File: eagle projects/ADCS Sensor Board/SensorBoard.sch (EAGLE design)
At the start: 128 parts, among them Q3 CSTCR4M00G15L99, Q5 32.768kHz, U10 LMV321, U2 ADS7841E_2K5, U3 LMV321, U5 ADS7841E_2K5, U6 REF194GSZ-REEL7, U7 TLV9054IDR, U8 LMV321

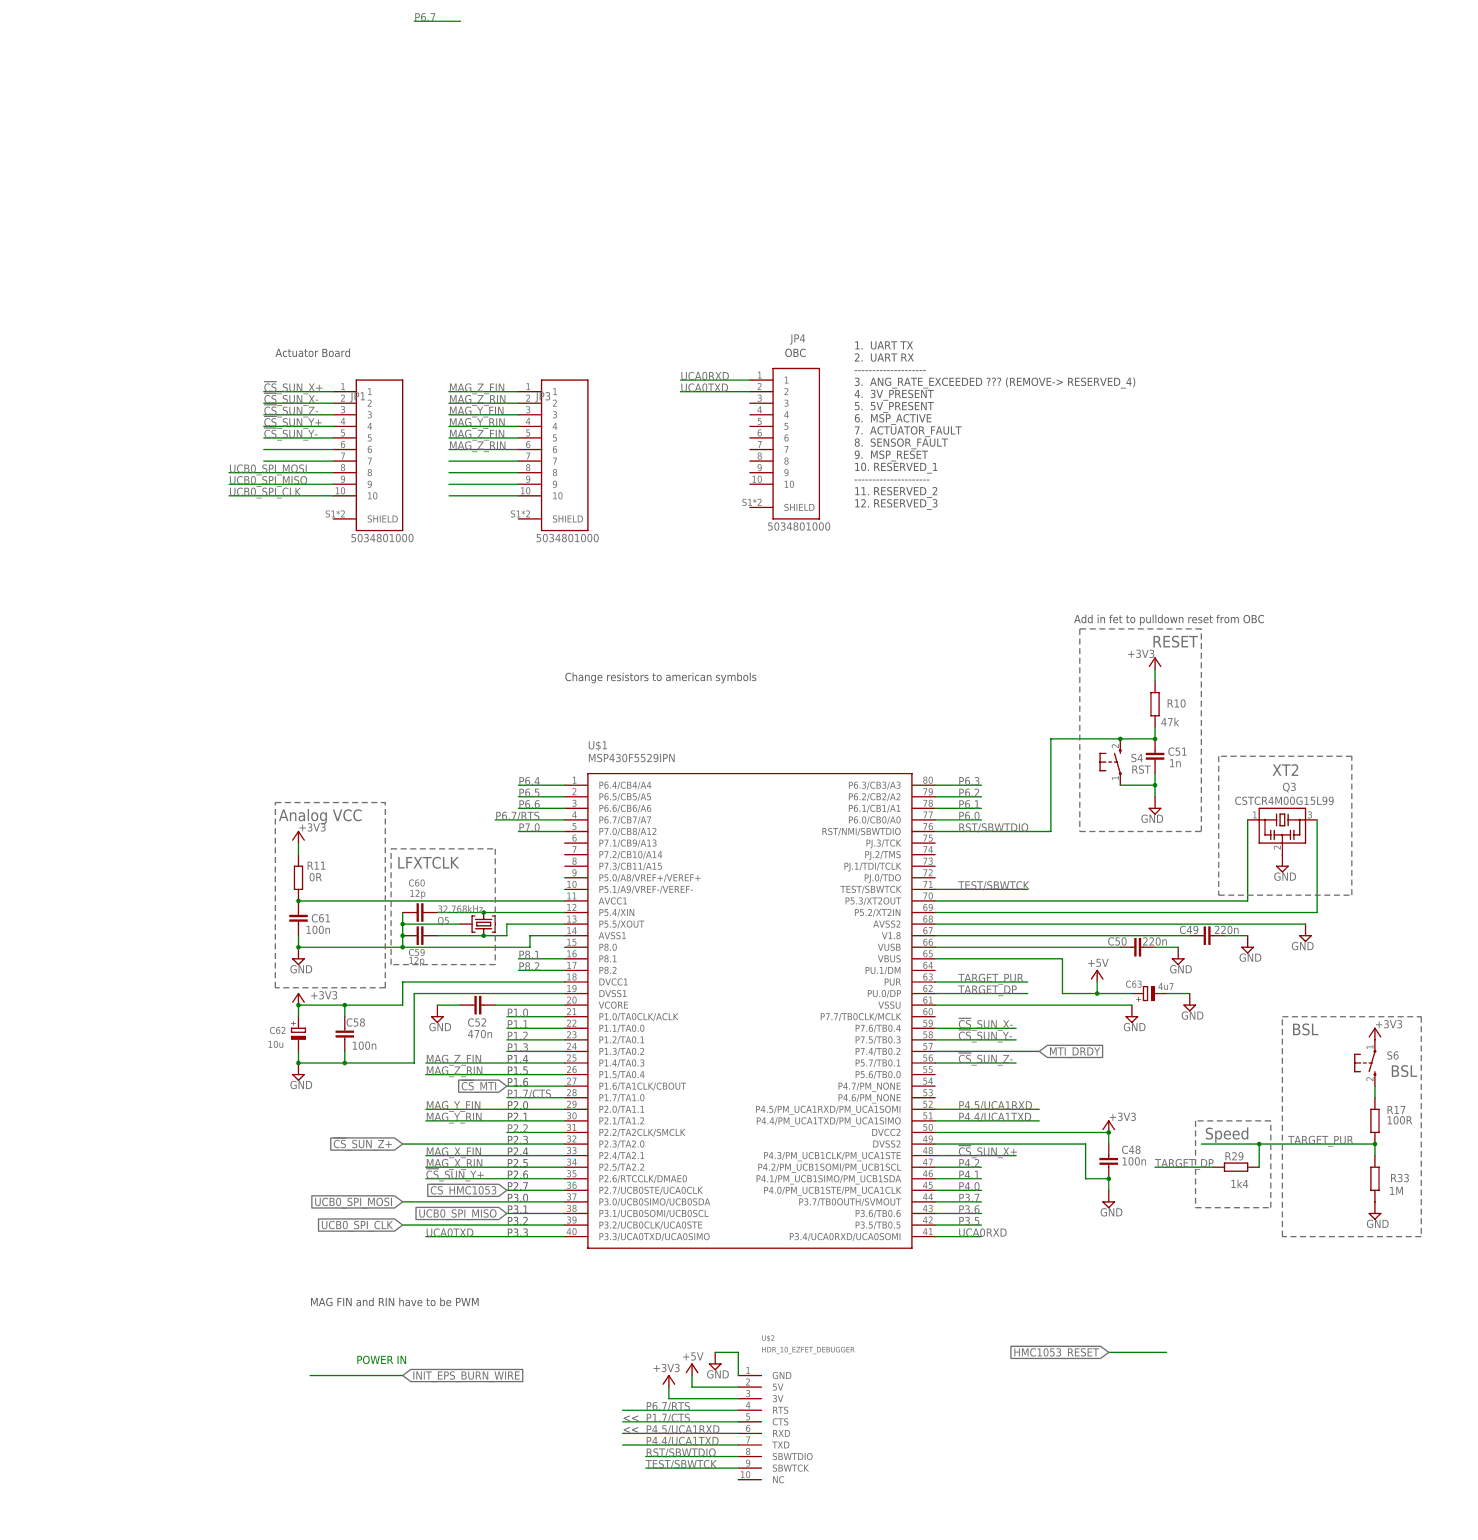
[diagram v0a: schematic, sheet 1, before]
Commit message: Renamed sensor board files. Added notes to schematic for remaining work
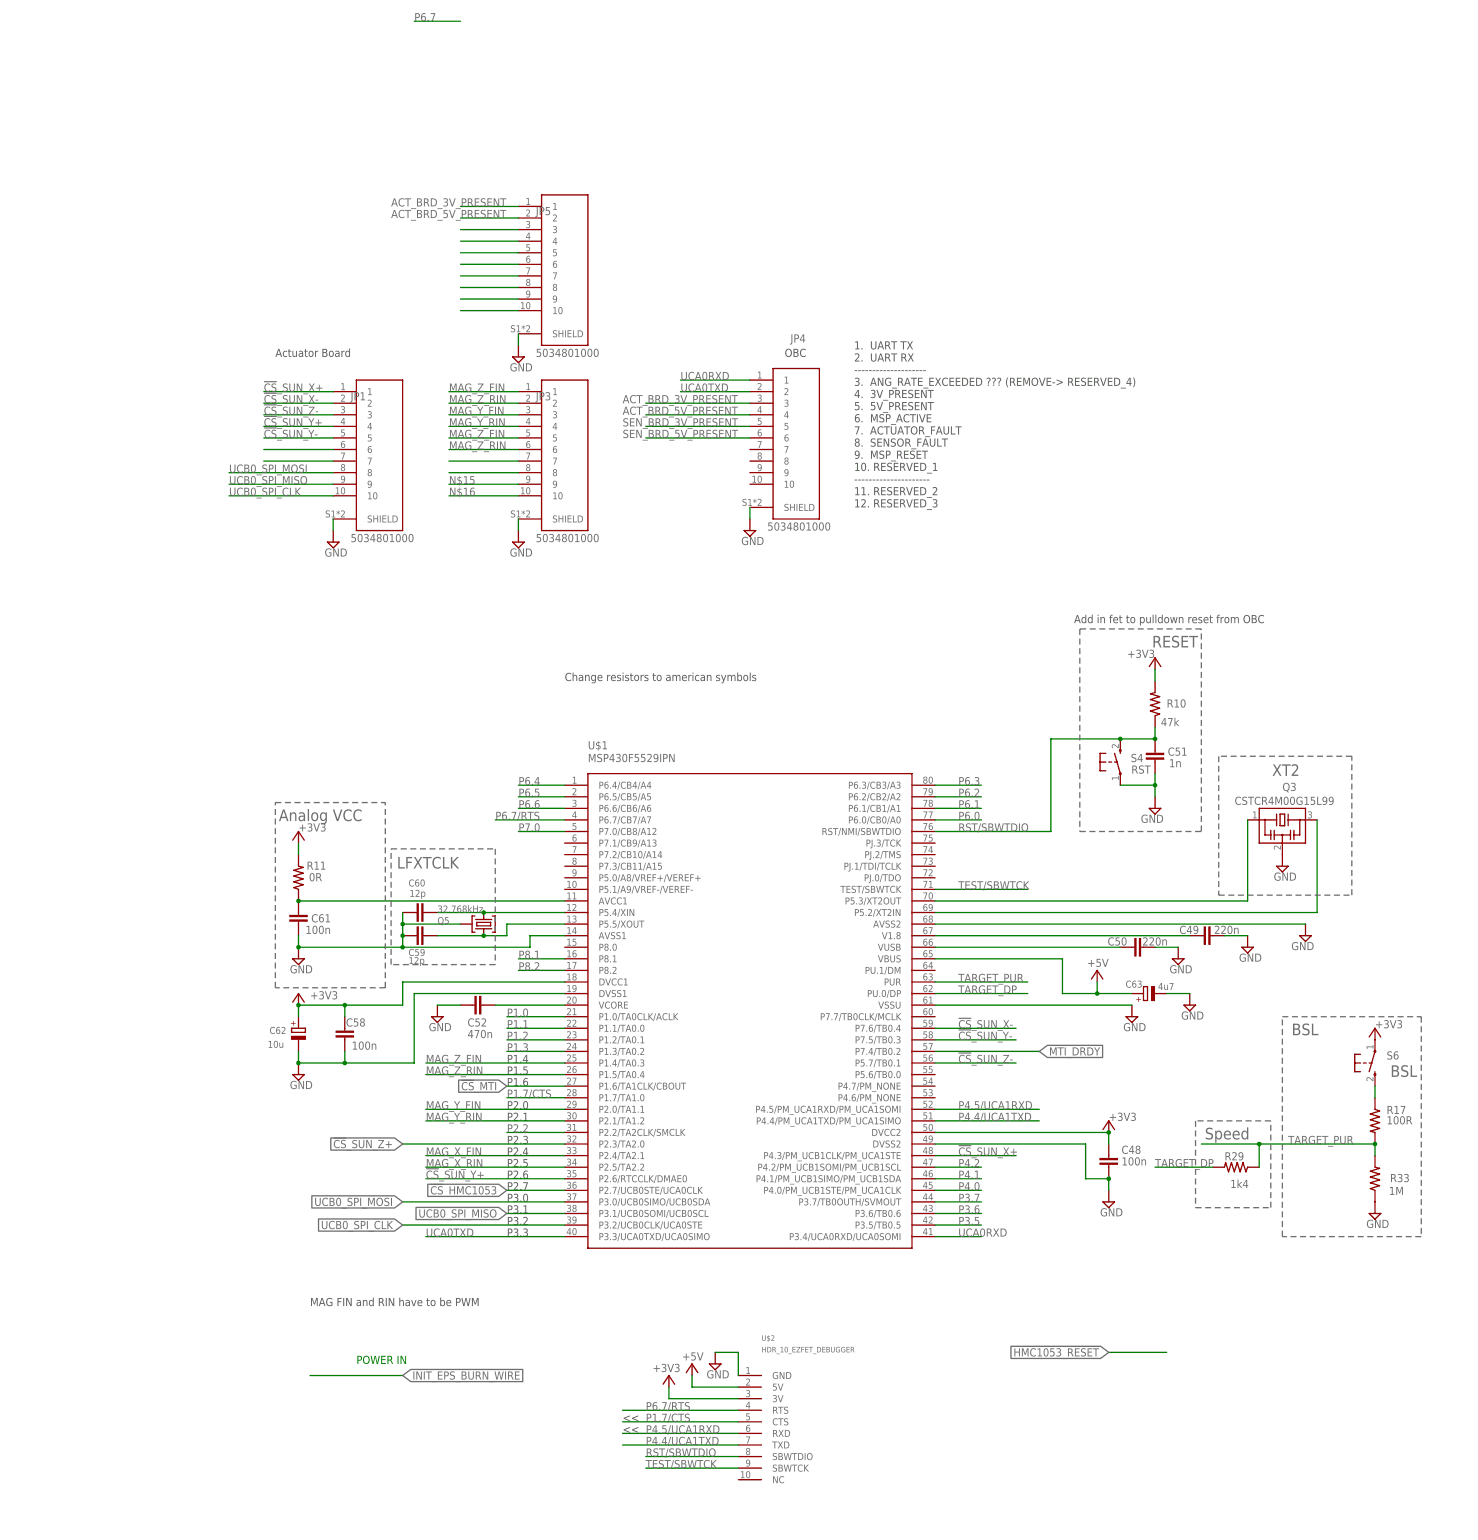
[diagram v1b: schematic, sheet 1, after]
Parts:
- added JP5: 5034801000, my_library:5034801000
- R10, R11, R17, R29, R33: device rcl:R-EU_RM0402 -> rcl:R-US_R0402
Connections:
- new net ACT_BRD_3V_PRESENT: JP4.3, JP5.1
- new net ACT_BRD_5V_PRESENT: JP4.4, JP5.2
- new net N$10: JP5.7
- new net N$17: JP5.8
- new net N$18: JP5.9
- new net N$19: JP5.10
- new net N$3: JP5.3
- new net N$4: JP5.4
- new net N$5: JP5.5
- new net N$9: JP5.6
- new net SEN_BRD_3V_PRESENT: JP4.5
- new net SEN_BRD_5V_PRESENT: JP4.6
- net GND: now also JP1.SHIELD, JP3.SHIELD, JP4.SHIELD, JP5.SHIELD
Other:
- note added: "Replace MTI-1 IMU with new 3-axis gyroscope"
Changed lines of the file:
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@@
 <part name="C49" library="rcl" deviceset="C-EU" device="CM0402" value="220n"/>
 <part name="C50" library="rcl" deviceset="C-EU" device="CM0402" value="220n"/>
-<part name="R10" library="rcl" deviceset="R-EU_" device="RM0402" value="47k"/>
+<part name="R10" library="rcl" library_urn="urn:adsk.eagle:library:334" deviceset="R-US_" device="R0402" package3d_urn="urn:adsk.eagle:package:23547/3" value="47k"/>
 <part name="C51" library="rcl" deviceset="C-EU" device="CM0402" value="1n"/>
 <part name="C52" library="rcl" deviceset="C-EU" device="CM0402" value="470n"/>
 <part name="C58" library="rcl" deviceset="C-EU" device="CM0402" value="100n"/>
-<part name="R11" library="rcl" deviceset="R-EU_" device="RM0402" value="0R"/>
+<part name="R11" library="rcl" library_urn="urn:adsk.eagle:library:334" deviceset="R-US_" device="R0402" package3d_urn="urn:adsk.eagle:package:23547/3" value="0R"/>
 <part name="C59" library="rcl" deviceset="C-EU" device="CM0402" value="12p"/>
 <part name="C60" library="rcl" deviceset="C-EU" device="CM0402" value="12p"/>
@@
 <part name="C61" library="rcl" deviceset="C-EU" device="CM0402" value="100n"/>
 <part name="C62" library="rcl" deviceset="CPOL-EU" device="A/3216-18R" value="10u"/>
-<part name="R17" library="rcl" deviceset="R-EU_" device="RM0402" value="100R"/>
+<part name="R17" library="rcl" library_urn="urn:adsk.eagle:library:334" deviceset="R-US_" device="R0402" package3d_urn="urn:adsk.eagle:package:23547/3" value="100R"/>
 <part name="S6" library="electricalmeter" deviceset="PB" device="" value="BSL"/>
-<part name="R29" library="rcl" deviceset="R-EU_" device="RM0402" value="1k4"/>
-<part name="R33" library="rcl" deviceset="R-EU_" device="RM0402" value="1M"/>
+<part name="R29" library="rcl" library_urn="urn:adsk.eagle:library:334" deviceset="R-US_" device="R0402" package3d_urn="urn:adsk.eagle:package:23547/3" value="1k4"/>
+<part name="R33" library="rcl" library_urn="urn:adsk.eagle:library:334" deviceset="R-US_" device="R0402" package3d_urn="urn:adsk.eagle:package:23547/3" value="1M"/>
 <part name="Q3" library="murata" deviceset="MURATA-FILTER_CSTCR" device="" technology="6M00G53Z" value="CSTCR4M00G15L99"/>
 <part name="+3V31" library="supply1" deviceset="+3V3" device=""/>
@@
 <part name="JP3" library="my_library" library_urn="urn:adsk.eagle:library:22876504" deviceset="5034801000" device="" package3d_urn="urn:adsk.eagle:package:23814316/2"/>
 <part name="JP4" library="my_library" library_urn="urn:adsk.eagle:library:22876504" deviceset="5034801000" device="" package3d_urn="urn:adsk.eagle:package:23814316/2"/>
+<part name="JP5" library="my_library" library_urn="urn:adsk.eagle:library:22876504" deviceset="5034801000" device="" package3d_urn="urn:adsk.eagle:package:23814316/2"/>
+<part name="SUPPLY3" library="supply2" library_urn="urn:adsk.eagle:library:372" deviceset="GND" device=""/>
+<part name="SUPPLY4" library="supply2" library_urn="urn:adsk.eagle:library:372" deviceset="GND" device=""/>
+<part name="SUPPLY6" library="supply2" library_urn="urn:adsk.eagle:library:372" deviceset="GND" device=""/>
+<part name="SUPPLY8" library="supply2" library_urn="urn:adsk.eagle:library:372" deviceset="GND" device=""/>
 </parts>
 <sheets>
@@
 <attribute name="VALUE" x="120.65" y="223.52" size="1.778" layer="96"/>
 </instance>
+<instance part="JP5" gate="G$1" x="76.2" y="279.4" smashed="yes">
+<attribute name="NAME" x="69.85" y="292.735" size="1.778" layer="95"/>
+<attribute name="VALUE" x="69.85" y="261.62" size="1.778" layer="96"/>
+</instance>
+<instance part="SUPPLY3" gate="GND" x="66.04" y="261.62" smashed="yes">
+<attribute name="VALUE" x="64.135" y="258.445" size="1.778" layer="96"/>
+</instance>
+<instance part="SUPPLY4" gate="GND" x="25.4" y="220.98" smashed="yes">
+<attribute name="VALUE" x="23.495" y="217.805" size="1.778" layer="96"/>
+</instance>
+<instance part="SUPPLY6" gate="GND" x="66.04" y="220.98" smashed="yes">
+<attribute name="VALUE" x="64.135" y="217.805" size="1.778" layer="96"/>
+</instance>
+<instance part="SUPPLY8" gate="GND" x="116.84" y="223.52" smashed="yes">
+<attribute name="VALUE" x="114.935" y="220.345" size="1.778" layer="96"/>
+</instance>
 </instances>
 <busses>
@@
 <pinref part="SUPPLY2" gate="GND" pin="GND"/>
 </segment>
+<segment>
+<pinref part="SUPPLY3" gate="GND" pin="GND"/>
+<pinref part="JP5" gate="G$1" pin="SHIELD"/>
+<wire x1="66.04" y1="264.16" x2="66.04" y2="266.7" width="0.1524" layer="91"/>
+</segment>
+<segment>
+<pinref part="SUPPLY4" gate="GND" pin="GND"/>
+<pinref part="JP1" gate="G$1" pin="SHIELD"/>
+<wire x1="25.4" y1="223.52" x2="25.4" y2="226.06" width="0.1524" layer="91"/>
+</segment>
+<segment>
+<pinref part="SUPPLY6" gate="GND" pin="GND"/>
+<pinref part="JP3" gate="G$1" pin="SHIELD"/>
+<wire x1="66.04" y1="223.52" x2="66.04" y2="226.06" width="0.1524" layer="91"/>
+</segment>
+<segment>
+<pinref part="SUPPLY8" gate="GND" pin="GND"/>
+<pinref part="JP4" gate="G$1" pin="SHIELD"/>
+<wire x1="116.84" y1="226.06" x2="116.84" y2="228.6" width="0.1524" layer="91"/>
+</segment>
 </net>
 <net name="TARGET_DP" class="0">
@@
 <pinref part="JP3" gate="G$1" pin="9"/>
 <wire x1="66.04" y1="233.68" x2="50.8" y2="233.68" width="0.1524" layer="91"/>
+<label x="50.8" y="233.68" size="1.778" layer="95"/>
 </segment>
 </net>
@@
 <wire x1="50.8" y1="231.14" x2="66.04" y2="231.14" width="0.1524" layer="91"/>
 <pinref part="JP3" gate="G$1" pin="10"/>
+<label x="50.8" y="231.14" size="1.778" layer="95"/>
 </segment>
 </net>
@@
 <wire x1="116.84" y1="256.54" x2="101.6" y2="256.54" width="0.1524" layer="91"/>
 <label x="101.6" y="256.54" size="1.778" layer="95"/>
+</segment>
+</net>
+<net name="ACT_BRD_3V_PRESENT" class="0">
+<segment>
+<pinref part="JP5" gate="G$1" pin="1"/>
+<wire x1="66.04" y1="294.64" x2="53.34" y2="294.64" width="0.1524" layer="91"/>
+<label x="38.1" y="294.64" size="1.778" layer="95"/>
+</segment>
+<segment>
+<pinref part="JP4" gate="G$1" pin="3"/>
+<wire x1="116.84" y1="251.46" x2="93.98" y2="251.46" width="0.1524" layer="91"/>
+<label x="88.9" y="251.46" size="1.778" layer="95"/>
+</segment>
+</net>
+<net name="ACT_BRD_5V_PRESENT" class="0">
+<segment>
+<pinref part="JP5" gate="G$1" pin="2"/>
+<wire x1="66.04" y1="292.1" x2="53.34" y2="292.1" width="0.1524" layer="91"/>
+<label x="38.1" y="292.1" size="1.778" layer="95"/>
+</segment>
+<segment>
+<wire x1="116.84" y1="248.92" x2="93.98" y2="248.92" width="0.1524" layer="91"/>
+<pinref part="JP4" gate="G$1" pin="4"/>
+<label x="88.9" y="248.92" size="1.778" layer="95"/>
+</segment>
+</net>
+<net name="N$3" class="0">
+<segment>
+<pinref part="JP5" gate="G$1" pin="3"/>
+<wire x1="66.04" y1="289.56" x2="53.34" y2="289.56" width="0.1524" layer="91"/>
+</segment>
+</net>
+<net name="N$4" class="0">
+<segment>
+<pinref part="JP5" gate="G$1" pin="4"/>
+<wire x1="66.04" y1="287.02" x2="53.34" y2="287.02" width="0.1524" layer="91"/>
+</segment>
+</net>
+<net name="N$5" class="0">
+<segment>
+<pinref part="JP5" gate="G$1" pin="5"/>
+<wire x1="66.04" y1="284.48" x2="53.34" y2="284.48" width="0.1524" layer="91"/>
+</segment>
+</net>
+<net name="N$9" class="0">
+<segment>
+<wire x1="53.34" y1="281.94" x2="66.04" y2="281.94" width="0.1524" layer="91"/>
+<pinref part="JP5" gate="G$1" pin="6"/>
+</segment>
+</net>
+<net name="N$10" class="0">
+<segment>
+<pinref part="JP5" gate="G$1" pin="7"/>
+<wire x1="66.04" y1="279.4" x2="53.34" y2="279.4" width="0.1524" layer="91"/>
+</segment>
+</net>
+<net name="N$17" class="0">
+<segment>
+<pinref part="JP5" gate="G$1" pin="8"/>
+<wire x1="66.04" y1="276.86" x2="53.34" y2="276.86" width="0.1524" layer="91"/>
+</segment>
+</net>
+<net name="N$18" class="0">
+<segment>
+<pinref part="JP5" gate="G$1" pin="9"/>
+<wire x1="53.34" y1="274.32" x2="66.04" y2="274.32" width="0.1524" layer="91"/>
+</segment>
+</net>
+<net name="N$19" class="0">
+<segment>
+<pinref part="JP5" gate="G$1" pin="10"/>
+<wire x1="53.34" y1="271.78" x2="66.04" y2="271.78" width="0.1524" layer="91"/>
+</segment>
+</net>
+<net name="SEN_BRD_3V_PRESENT" class="0">
+<segment>
+<pinref part="JP4" gate="G$1" pin="5"/>
+<wire x1="116.84" y1="246.38" x2="93.98" y2="246.38" width="0.1524" layer="91"/>
+<label x="88.9" y="246.38" size="1.778" layer="95"/>
+</segment>
+</net>
+<net name="SEN_BRD_5V_PRESENT" class="0">
+<segment>
+<pinref part="JP4" gate="G$1" pin="6"/>
+<wire x1="116.84" y1="243.84" x2="93.98" y2="243.84" width="0.1524" layer="91"/>
+<label x="88.9" y="243.84" size="1.778" layer="95"/>
 </segment>
 </net>
@@
 <sheet>
 <plain>
+<text x="114.3" y="152.4" size="1.778" layer="97">Replace MTI-1 IMU with new 3-axis gyroscope</text>
 </plain>
 <instances>
